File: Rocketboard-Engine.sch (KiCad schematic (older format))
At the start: 31 parts, among them IC1 STM32L072CBT6, J1 SWD Port, J2 USB_C_Receptacle_USB2.0, J3 Conn_01x20, J4 Conn_01x20, Q1 BSS138, U1 USBLC6-2SC6, U2 AMS1117-3.3

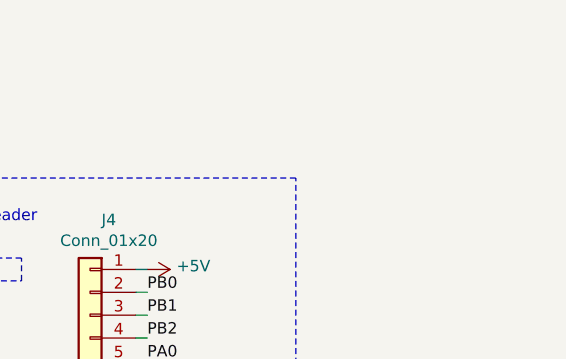
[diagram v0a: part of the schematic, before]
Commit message: Added silkscreen, fixed some placements, and generated gerbers
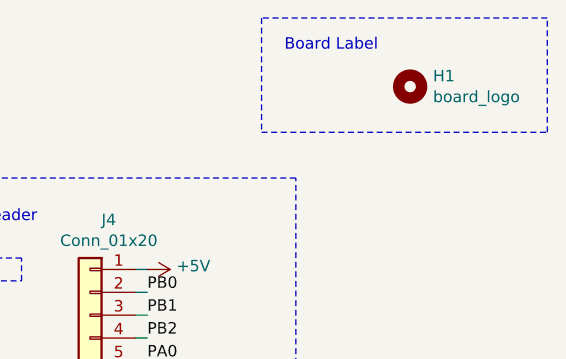
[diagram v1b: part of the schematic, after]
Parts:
- added H1: board_logo, Rocketboard-Engine:board-title, symbol Mechanical:MountingHole
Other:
- note added: "Board Label"
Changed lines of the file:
@@
 Wire Wire Line
 	9100 1800 9150 1800
+$Comp
+L Mechanical:MountingHole H1
+U 1 1 61A6311A
+P 10300 1000
+F 0 "H1" H 10400 1046 50  0000 L CNN
+F 1 "board_logo" H 10400 955 50  0000 L CNN
+F 2 "Rocketboard-Engine:board-title" H 10300 1000 50  0001 C CNN
+F 3 "~" H 10300 1000 50  0001 C CNN
+	1    10300 1000
+	1    0    0    -1
+$EndComp
+Text Notes 9750 850  0    50   ~ 0
+Board Label
+Wire Notes Line
+	9650 700  9650 1200
+Wire Notes Line
+	9650 1200 10900 1200
+Wire Notes Line
+	10900 1200 10900 700
+Wire Notes Line
+	10900 700  9650 700
 $EndSCHEMATC
